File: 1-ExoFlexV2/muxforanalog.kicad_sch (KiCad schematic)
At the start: 6 parts

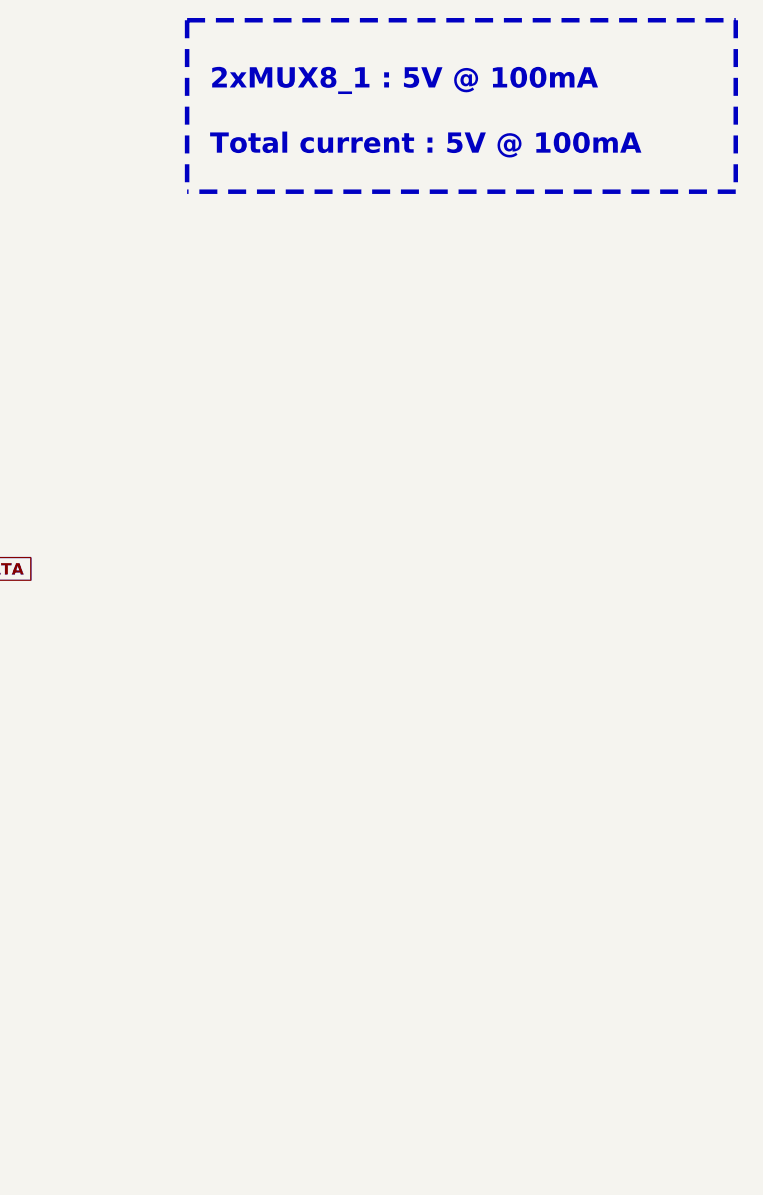
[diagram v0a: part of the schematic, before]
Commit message: Chokes et RC
- Ajout des RF chokes
- Changement des résistance pour 0805
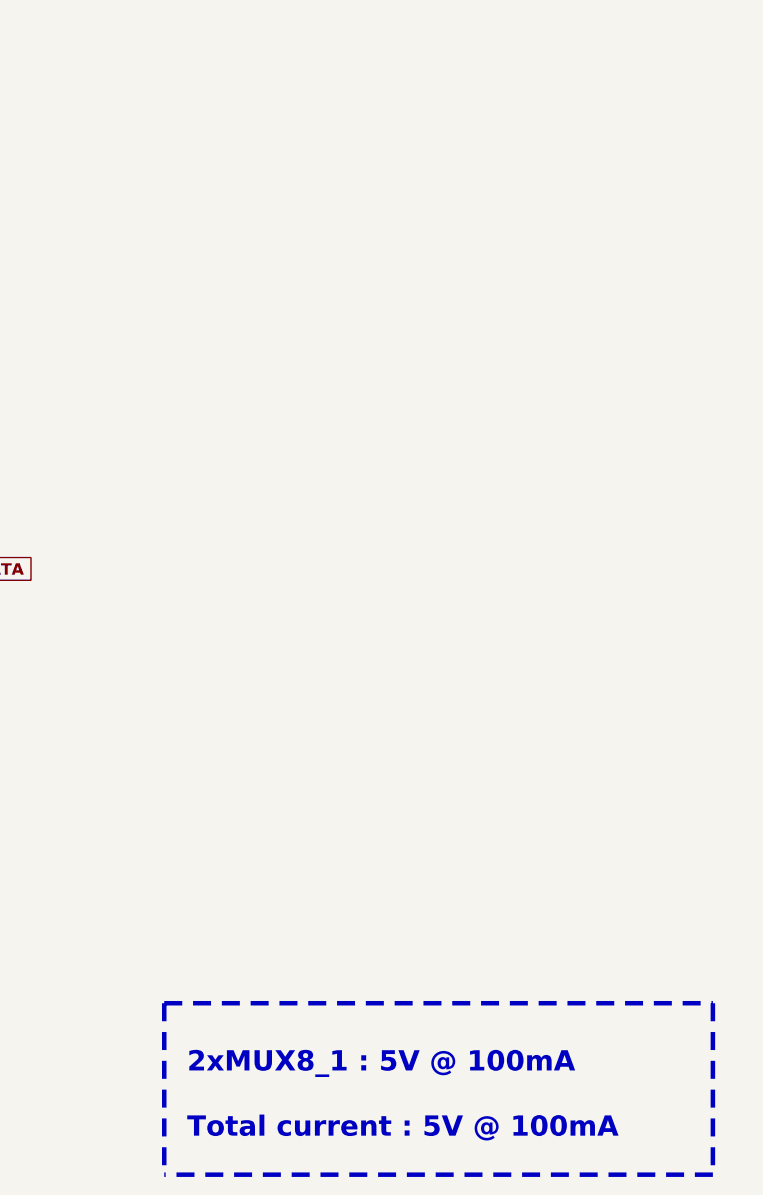
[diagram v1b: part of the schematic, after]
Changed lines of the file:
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@@
     (stroke (width 0) (type default) (color 0 0 0 0))
   )
-  (polyline (pts (xy 281.94 54.61) (xy 220.98 54.61))
+  (polyline (pts (xy 279.4 163.83) (xy 218.44 163.83))
     (stroke (width 0.5) (type dash) (color 255 148 44 1))
   )
@@
     (stroke (width 0) (type default) (color 0 0 0 0))
   )
-  (polyline (pts (xy 220.98 35.56) (xy 220.98 54.61))
+  (polyline (pts (xy 218.44 144.78) (xy 218.44 163.83))
     (stroke (width 0.5) (type dash) (color 255 148 44 1))
   )
@@
     (stroke (width 0) (type default) (color 0 0 0 0))
   )
-  (polyline (pts (xy 281.94 35.56) (xy 281.94 54.61))
+  (polyline (pts (xy 279.4 144.78) (xy 279.4 163.83))
     (stroke (width 0.5) (type dash) (color 255 148 44 1))
   )
@@
     (stroke (width 0) (type default) (color 0 0 0 0))
   )
-  (polyline (pts (xy 220.98 35.56) (xy 281.94 35.56))
+  (polyline (pts (xy 218.44 144.78) (xy 279.4 144.78))
     (stroke (width 0.5) (type dash) (color 255 148 44 1))
   )
@@
     (stroke (width 0) (type default) (color 0 0 0 0))
   )
-  (text "2xMUX8_1 : 5V @ 100mA\n\nTotal current : 5V @ 100mA" (at 223.52 50.8 0)
+  (text "2xMUX8_1 : 5V @ 100mA\n\nTotal current : 5V @ 100mA" (at 220.98 160.02 0)
     (effects (font (size 2.25 2.25) (thickness 0.5) bold) (justify left bottom))
   )

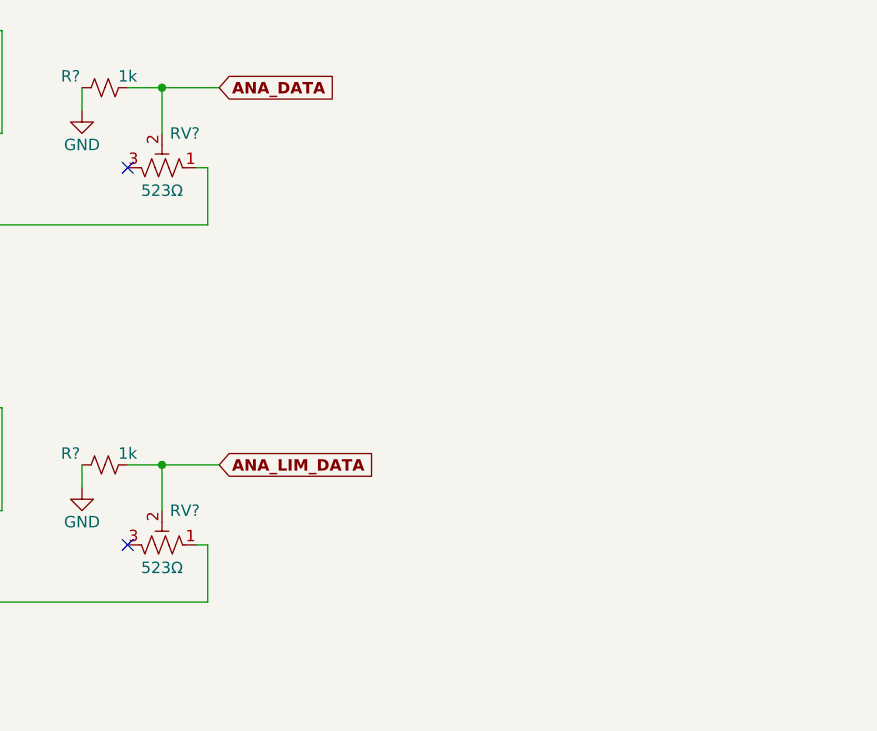
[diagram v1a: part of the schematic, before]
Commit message: Trimmer et jumper
-Changement de symbole de jumper
-Ajout des des trimmer aux endroits nécessaires
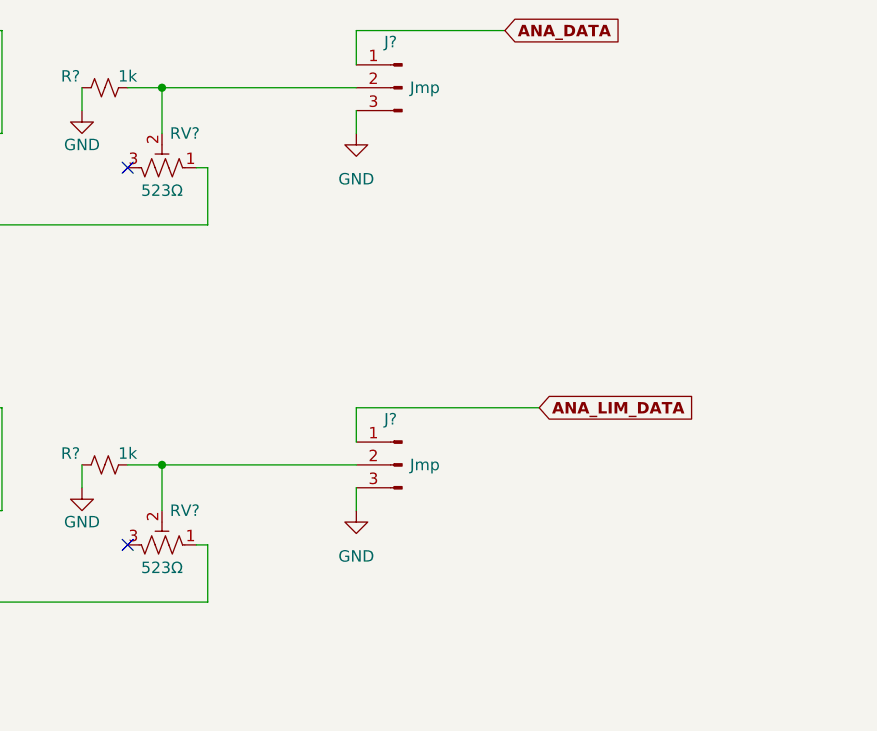
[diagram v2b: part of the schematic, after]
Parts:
- added J? (x2): Jmp, symbol Connector:Conn_01x03_Male
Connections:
- net ANA_DATA: now also J?.1 (Pin_1); no longer R?.2, RV?.2
- net ANA_LIM_DATA: now also J?.1 (Pin_1); no longer R?.2, RV?.2
- net GND: now also J?.3 (Pin_3), J?.3 (Pin_3)
- new net: J?.2 (Pin_2), R?.2, RV?.2 (x2)
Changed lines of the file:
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@@
   (junction (at 180.34 96.52) (diameter 0) (color 0 0 0 0)
   )
+  (junction (at 180.34 54.61) (diameter 0) (color 0 0 0 0)
+  )
   (junction (at 100.33 62.23) (diameter 0) (color 0 0 0 0)
   )
   (junction (at 102.87 59.69) (diameter 0) (color 0 0 0 0)
-  )
-  (junction (at 180.34 54.61) (diameter 0) (color 0 0 0 0)
   )
   (junction (at 156.21 59.69) (diameter 0) (color 0 0 0 0)
@@
     (stroke (width 0) (type default) (color 0 0 0 0))
   )
+  (wire (pts (xy 201.93 93.98) (xy 201.93 90.17))
+    (stroke (width 0) (type default) (color 0 0 0 0))
+  )
   (wire (pts (xy 185.42 105.41) (xy 185.42 111.76))
     (stroke (width 0) (type default) (color 0 0 0 0))
@@
     (stroke (width 0) (type default) (color 0 0 0 0))
   )
-  (wire (pts (xy 180.34 54.61) (xy 186.69 54.61))
-    (stroke (width 0) (type default) (color 0 0 0 0))
-  )
   (wire (pts (xy 95.25 64.77) (xy 97.79 64.77))
     (stroke (width 0) (type default) (color 0 0 0 0))
   )
+  (wire (pts (xy 201.93 48.26) (xy 218.44 48.26))
+    (stroke (width 0) (type default) (color 0 0 0 0))
+  )
   (wire (pts (xy 171.45 54.61) (xy 171.45 57.15))
     (stroke (width 0) (type default) (color 0 0 0 0))
@@
     (stroke (width 0) (type default) (color 0 0 0 0))
   )
+  (wire (pts (xy 201.93 99.06) (xy 201.93 101.6))
+    (stroke (width 0) (type default) (color 0 0 0 0))
+  )
   (wire (pts (xy 180.34 96.52) (xy 180.34 101.6))
     (stroke (width 0) (type default) (color 0 0 0 0))
@@
   )
   (wire (pts (xy 102.87 59.69) (xy 135.89 59.69))
+    (stroke (width 0) (type default) (color 0 0 0 0))
+  )
+  (wire (pts (xy 201.93 57.15) (xy 201.93 59.69))
+    (stroke (width 0) (type default) (color 0 0 0 0))
+  )
+  (wire (pts (xy 180.34 96.52) (xy 201.93 96.52))
     (stroke (width 0) (type default) (color 0 0 0 0))
   )
@@
     (stroke (width 0) (type default) (color 0 0 0 0))
   )
+  (wire (pts (xy 201.93 52.07) (xy 201.93 48.26))
+    (stroke (width 0) (type default) (color 0 0 0 0))
+  )
   (polyline (pts (xy 218.44 144.78) (xy 279.4 144.78))
     (stroke (width 0.5) (type dash) (color 255 148 44 1))
@@
     (stroke (width 0) (type default) (color 0 0 0 0))
   )
-  (wire (pts (xy 180.34 96.52) (xy 186.69 96.52))
-    (stroke (width 0) (type default) (color 0 0 0 0))
-  )
   (wire (pts (xy 97.79 106.68) (xy 135.89 106.68))
     (stroke (width 0) (type default) (color 0 0 0 0))
@@
     (stroke (width 0) (type default) (color 0 0 0 0))
   )
+  (wire (pts (xy 180.34 54.61) (xy 201.93 54.61))
+    (stroke (width 0) (type default) (color 0 0 0 0))
+  )
   (wire (pts (xy 162.56 90.17) (xy 162.56 101.6))
     (stroke (width 0) (type default) (color 0 0 0 0))
@@
   )
   (wire (pts (xy 100.33 104.14) (xy 135.89 104.14))
+    (stroke (width 0) (type default) (color 0 0 0 0))
+  )
+  (wire (pts (xy 201.93 90.17) (xy 222.25 90.17))
     (stroke (width 0) (type default) (color 0 0 0 0))
   )
@@
     (effects (font (size 2.25 2.25) (thickness 0.5) bold) (justify left bottom))
   )
-  (global_label "ANA_LIM_DATA" (shape input) (at 186.69 96.52 0) (fields_autoplaced)
+  (global_label "ANA_LIM_DATA" (shape input) (at 222.25 90.17 0) (fields_autoplaced)
     (effects (font (size 1.27 1.27) bold) (justify left))
-    (property "Intersheet References" "${INTERSHEET_REFS}" (id 0) (at 202.4259 96.393 0)
+    (property "Intersheet References" "${INTERSHEET_REFS}" (id 0) (at 237.9859 90.043 0)
       (effects (font (size 1.27 1.27) bold) (justify left) hide)
     )
@@
     )
   )
-  (global_label "ANA_DATA" (shape input) (at 186.69 54.61 0) (fields_autoplaced)
+  (global_label "ANA_DATA" (shape input) (at 218.44 48.26 0) (fields_autoplaced)
     (effects (font (size 1.27 1.27) bold) (justify left))
-    (property "Intersheet References" "${INTERSHEET_REFS}" (id 0) (at 198.374 54.483 0)
+    (property "Intersheet References" "${INTERSHEET_REFS}" (id 0) (at 230.124 48.133 0)
       (effects (font (size 1.27 1.27) bold) (justify left) hide)
     )
@@
     (pin "1")
   )
+  (symbol (lib_id "power:GND") (at 201.93 59.69 0) (unit 1)
+    (in_bom yes) (on_board yes) (fields_autoplaced)
+    (property "Reference" "#PWR?" (id 0) (at 201.93 66.04 0)
+      (effects (font (size 1.27 1.27)) hide)
+    )
+    (property "Value" "GND" (id 1) (at 201.93 64.77 0))
+    (property "Footprint" "" (id 2) (at 201.93 59.69 0)
+      (effects (font (size 1.27 1.27)) hide)
+    )
+    (property "Datasheet" "" (id 3) (at 201.93 59.69 0)
+      (effects (font (size 1.27 1.27)) hide)
+    )
+    (pin "1")
+  )
   (symbol (lib_id "Device:R_Potentiometer_Trim_US") (at 180.34 105.41 270) (mirror x) (unit 1)
     (in_bom yes) (on_board yes)
@@
     (pin "2")
   )
+  (symbol (lib_id "Connector:Conn_01x03_Male") (at 207.01 54.61 0) (mirror y) (unit 1)
+    (in_bom yes) (on_board yes)
+    (property "Reference" "J?" (id 0) (at 205.74 49.53 0))
+    (property "Value" "Jmp" (id 1) (at 209.55 54.61 0))
+    (property "Footprint" "" (id 2) (at 207.01 54.61 0)
+      (effects (font (size 1.27 1.27)) hide)
+    )
+    (property "Datasheet" "~" (id 3) (at 207.01 54.61 0)
+      (effects (font (size 1.27 1.27)) hide)
+    )
+    (pin "1")
+    (pin "2")
+    (pin "3")
+  )
+  (symbol (lib_id "Connector:Conn_01x03_Male") (at 207.01 96.52 0) (mirror y) (unit 1)
+    (in_bom yes) (on_board yes)
+    (property "Reference" "J?" (id 0) (at 205.74 91.44 0))
+    (property "Value" "Jmp" (id 1) (at 209.55 96.52 0))
+    (property "Footprint" "" (id 2) (at 207.01 96.52 0)
+      (effects (font (size 1.27 1.27)) hide)
+    )
+    (property "Datasheet" "~" (id 3) (at 207.01 96.52 0)
+      (effects (font (size 1.27 1.27)) hide)
+    )
+    (pin "1")
+    (pin "2")
+    (pin "3")
+  )
   (symbol (lib_id "power:GND") (at 156.21 127 0) (unit 1)
     (in_bom yes) (on_board yes) (fields_autoplaced)
@@
       (effects (font (size 1.27 1.27)) hide)
     )
+    (pin "1")
+  )
+  (symbol (lib_id "power:GND") (at 201.93 101.6 0) (unit 1)
+    (in_bom yes) (on_board yes) (fields_autoplaced)
+    (property "Reference" "#PWR?" (id 0) (at 201.93 107.95 0)
+      (effects (font (size 1.27 1.27)) hide)
+    )
+    (property "Value" "GND" (id 1) (at 201.93 106.68 0))
+    (property "Footprint" "" (id 2) (at 201.93 101.6 0)
+      (effects (font (size 1.27 1.27)) hide)
+    )
+    (property "Datasheet" "" (id 3) (at 201.93 101.6 0)
+      (effects (font (size 1.27 1.27)) hide)
+    )

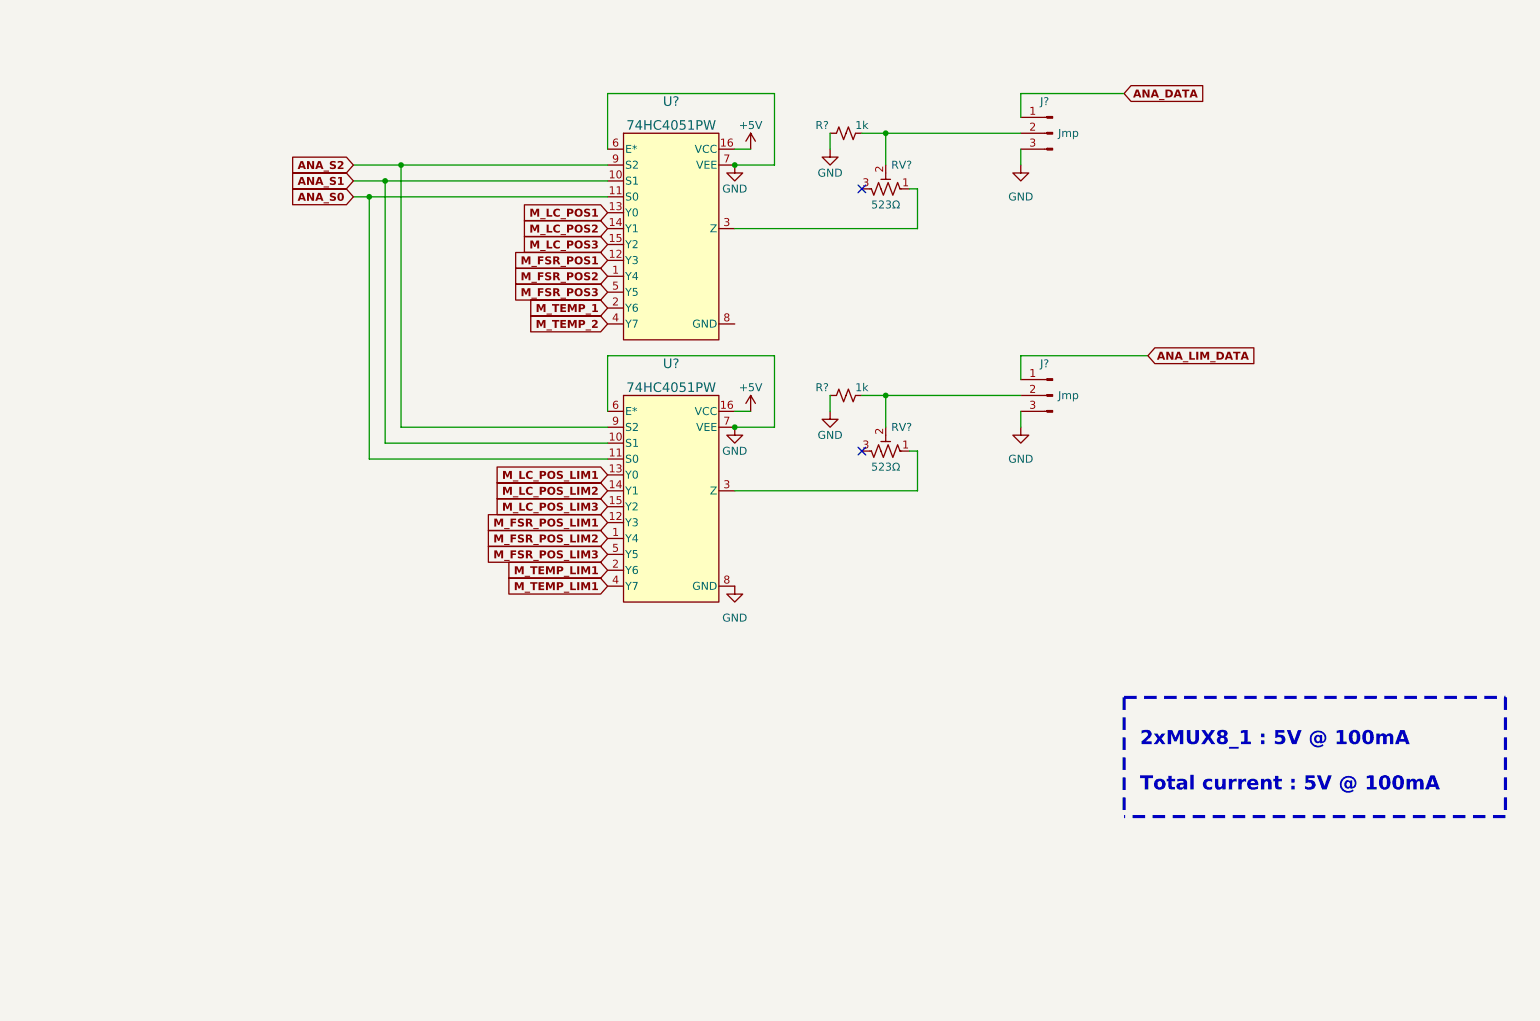
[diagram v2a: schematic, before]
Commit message: Test points et notes
- Ajout de tous les tests point nécessaires
-  Ajoute des sections de notes dans chaque page
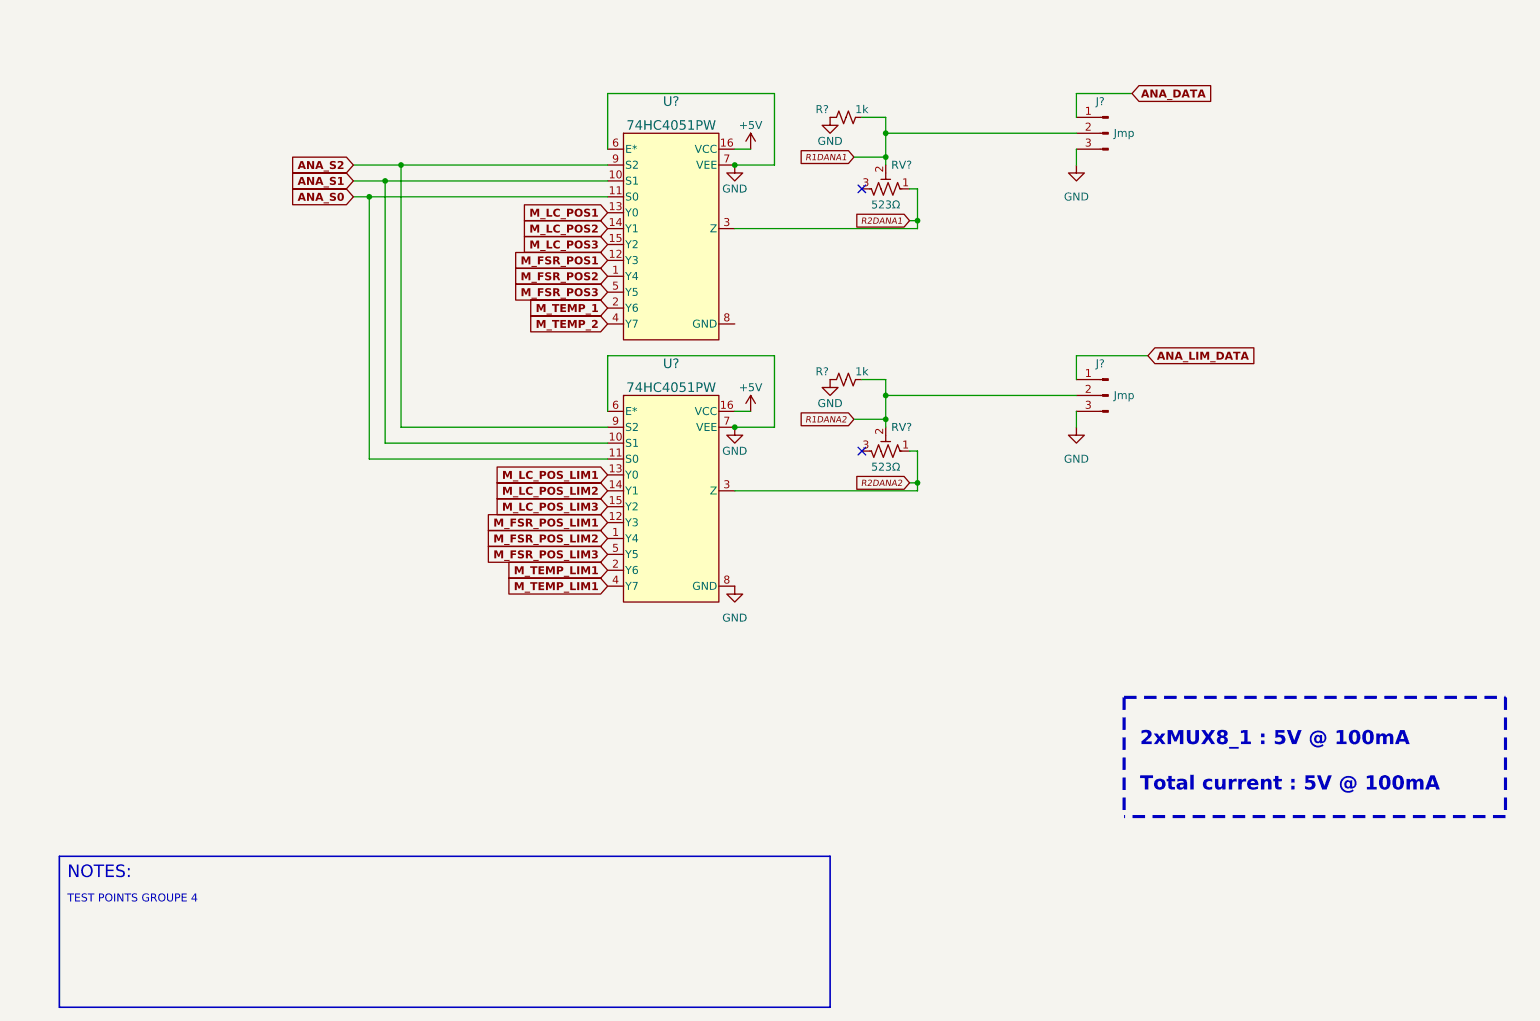
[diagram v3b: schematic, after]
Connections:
- net R1DANA2: now reaches J?.2 (Pin_2), R?.2, RV?.2
- net R2DANA2: now reaches RV?.1, U?.3 (Z)
- net R2DANA1: now reaches RV?.1, U?.3 (Z)
- net R1DANA1: now reaches J?.2 (Pin_2), R?.2, RV?.2
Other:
- note added: "NOTES:"
- note added: "TEST POINTS GROUPE 4"
- moved on the sheet: J?, R?
